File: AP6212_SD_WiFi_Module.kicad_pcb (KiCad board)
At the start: 2 copper layers, 24.6 x 23 mm, 21 parts, among them J1 Conn_Coaxial, J2 TF_Card, U1 AP6212, Y1 26MHz

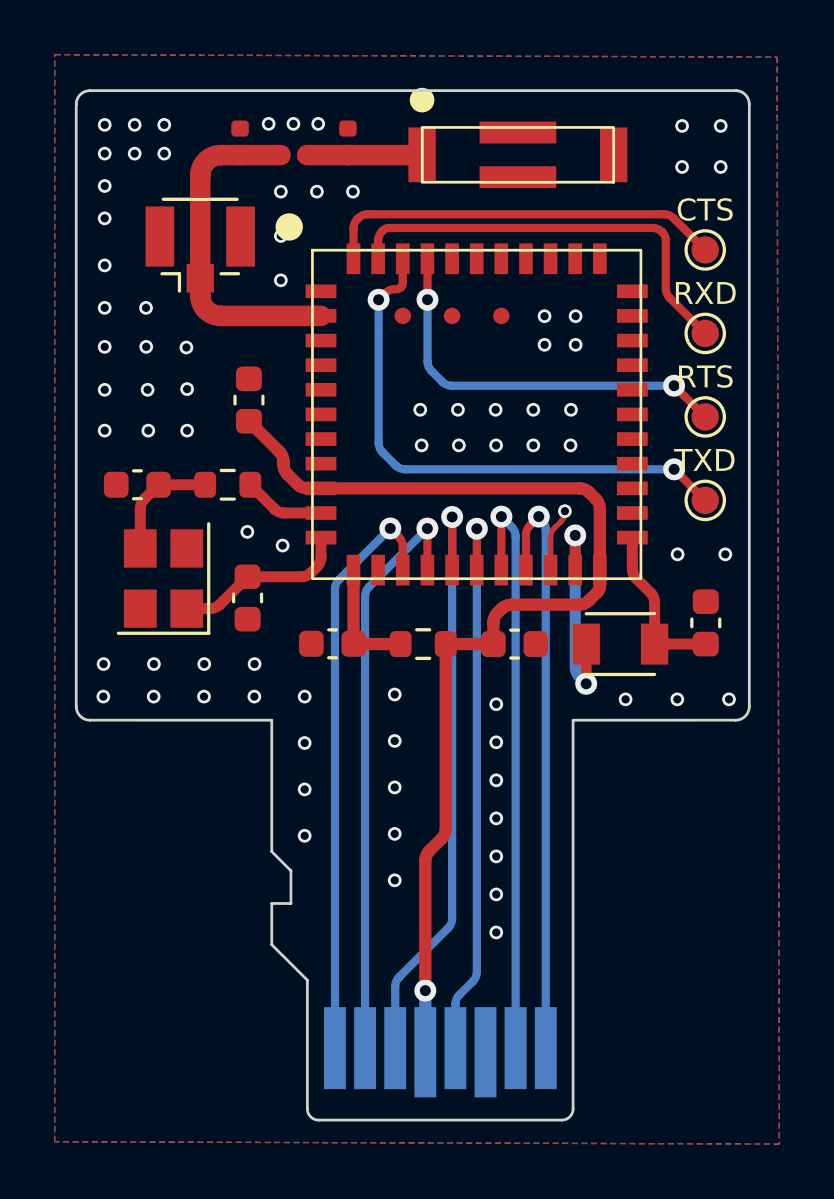
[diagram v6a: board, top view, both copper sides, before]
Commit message: feat: Optimized antenna layout and routing
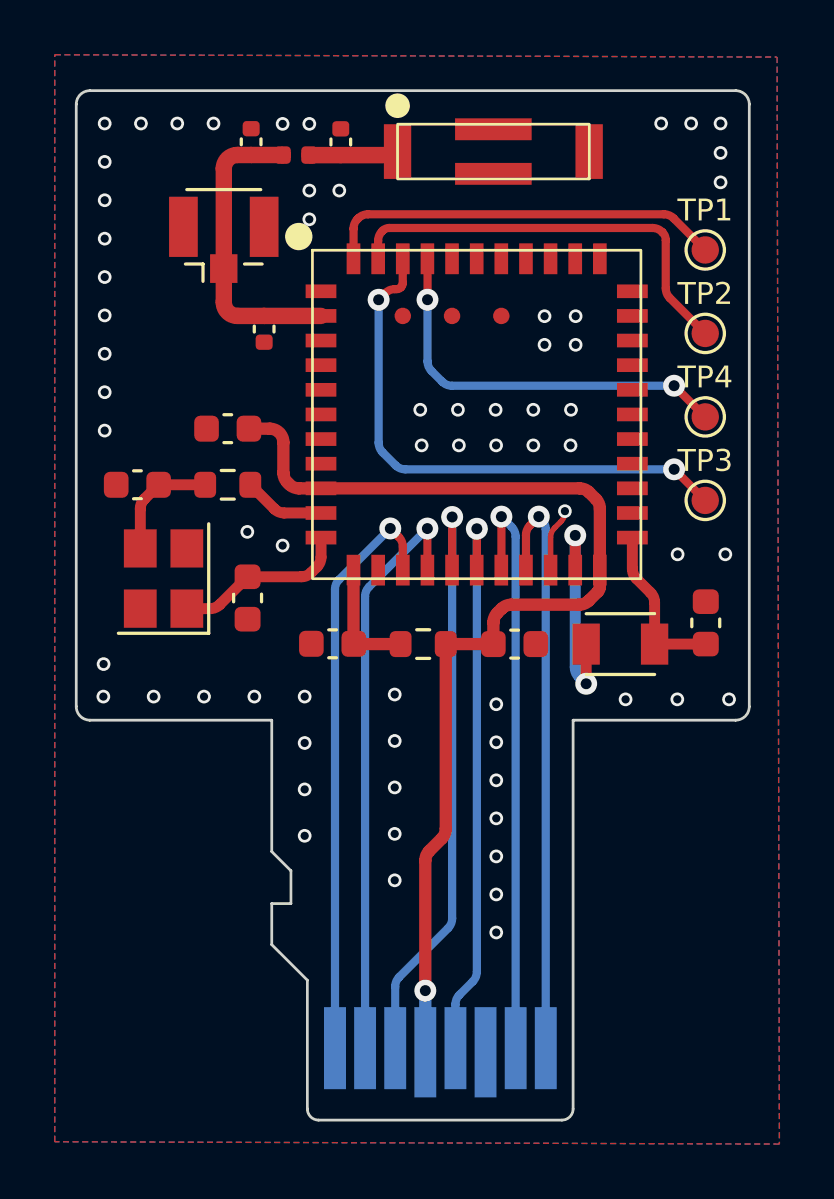
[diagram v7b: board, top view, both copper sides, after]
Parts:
- removed the L2 at (207.6, 108.9)
- removed L3: 3.3nH, Inductor_SMD:L_0402_1005Metric
- added C3: 3.3nH, Capacitor_SMD:C_0402_1005Metric, F.Cu at (207.4, 108.9)
- added C4: 3.3nH, Capacitor_SMD:C_0402_1005Metric, F.Cu at (204.1, 108.9)
- added C5: DNP, Capacitor_SMD:C_0402_1005Metric, F.Cu at (204.6, 115.7)
- moved C6 1.30 mm to (203.2, 119.3), turned to 0 degrees
- moved J1 0.93 mm to (203.1, 112.5)
- moved AE1 0.90 mm to (212.9, 109.2)
- moved L1 0.08 mm to (205.7, 109.4)
- renumbered C3 to C6, C4 to C7, C5 to C8, C6 to C9, L4 to L2, CTS to TP1, RXD to TP2, TXD to TP3, RTS to TP4
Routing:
- net Net-(J1-In): track 12.5 -> 11.1 mm
- net Net-(AE1-A): track 4.20 -> 3.28 mm
- net GND: vias 78 -> 65

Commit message: feat: Fine-tune the antenna layout and remove all teardrops
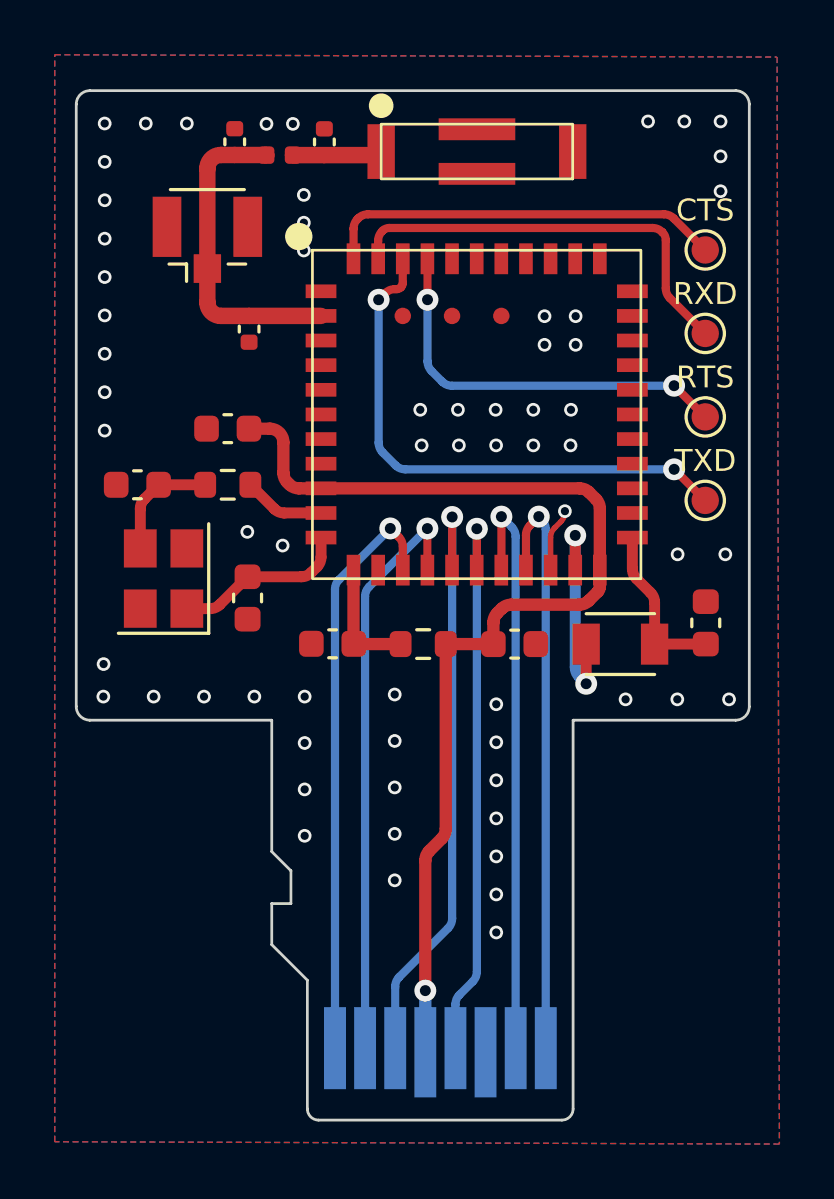
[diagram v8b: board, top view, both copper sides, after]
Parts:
- moved L1 0.60 mm to (205.1, 109.4)
- moved AE1 0.60 mm to (212.3, 109.2)
- moved C3 0.60 mm to (206.8, 108.9)
- moved C4 0.60 mm to (203.5, 108.9)
- moved J1 0.60 mm to (202.5, 112.5)
- moved C5 0.55 mm to (204.0, 115.7)
- renumbered TP1 to CTS, TP4 to RTS, TP2 to RXD, TP3 to TXD
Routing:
- net Net-(J1-In): track 11.1 -> 11.7 mm
- net GND: vias 65 -> 64
